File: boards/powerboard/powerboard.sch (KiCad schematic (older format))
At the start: 39 parts, among them J101 RXSM experiment connector, J102 Powerboard <-> Mainboard, J103 Cameraboard, J104 BLDC Motor, J105 BOOST, J106 Boost24V_EN, J107 24V_1, J108 24V_2, J109 24V_3, J110 BAT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

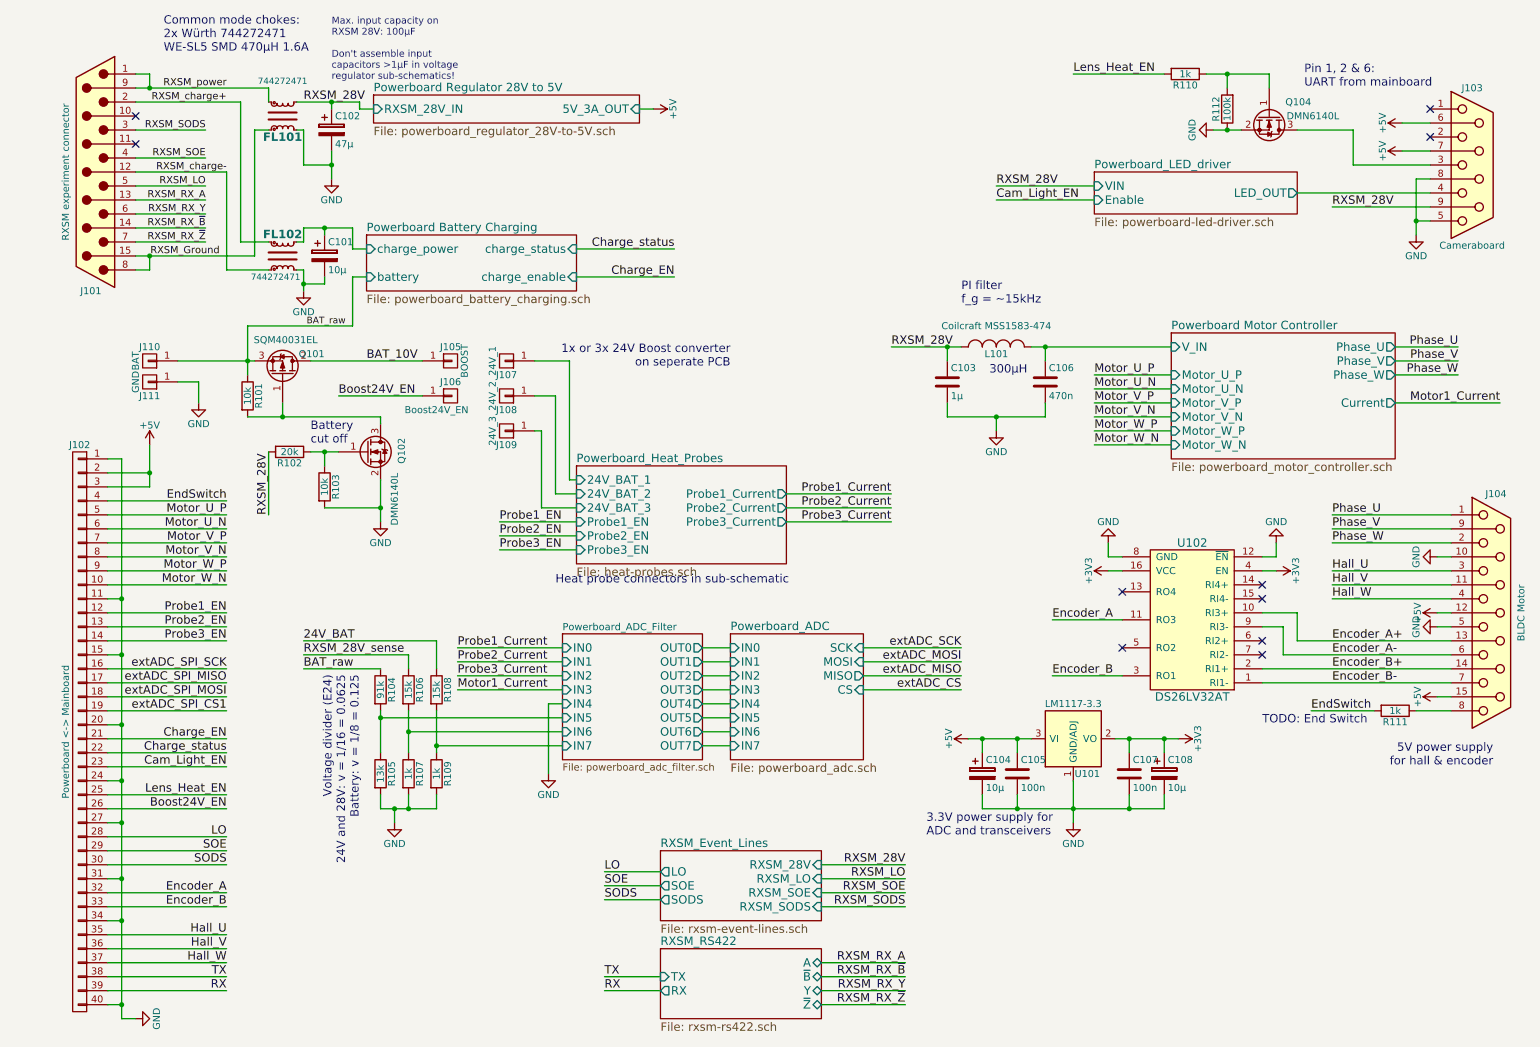
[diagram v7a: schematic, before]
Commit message: [powerboard] layout: parts placed; RS-422 termination added; various minor improvements
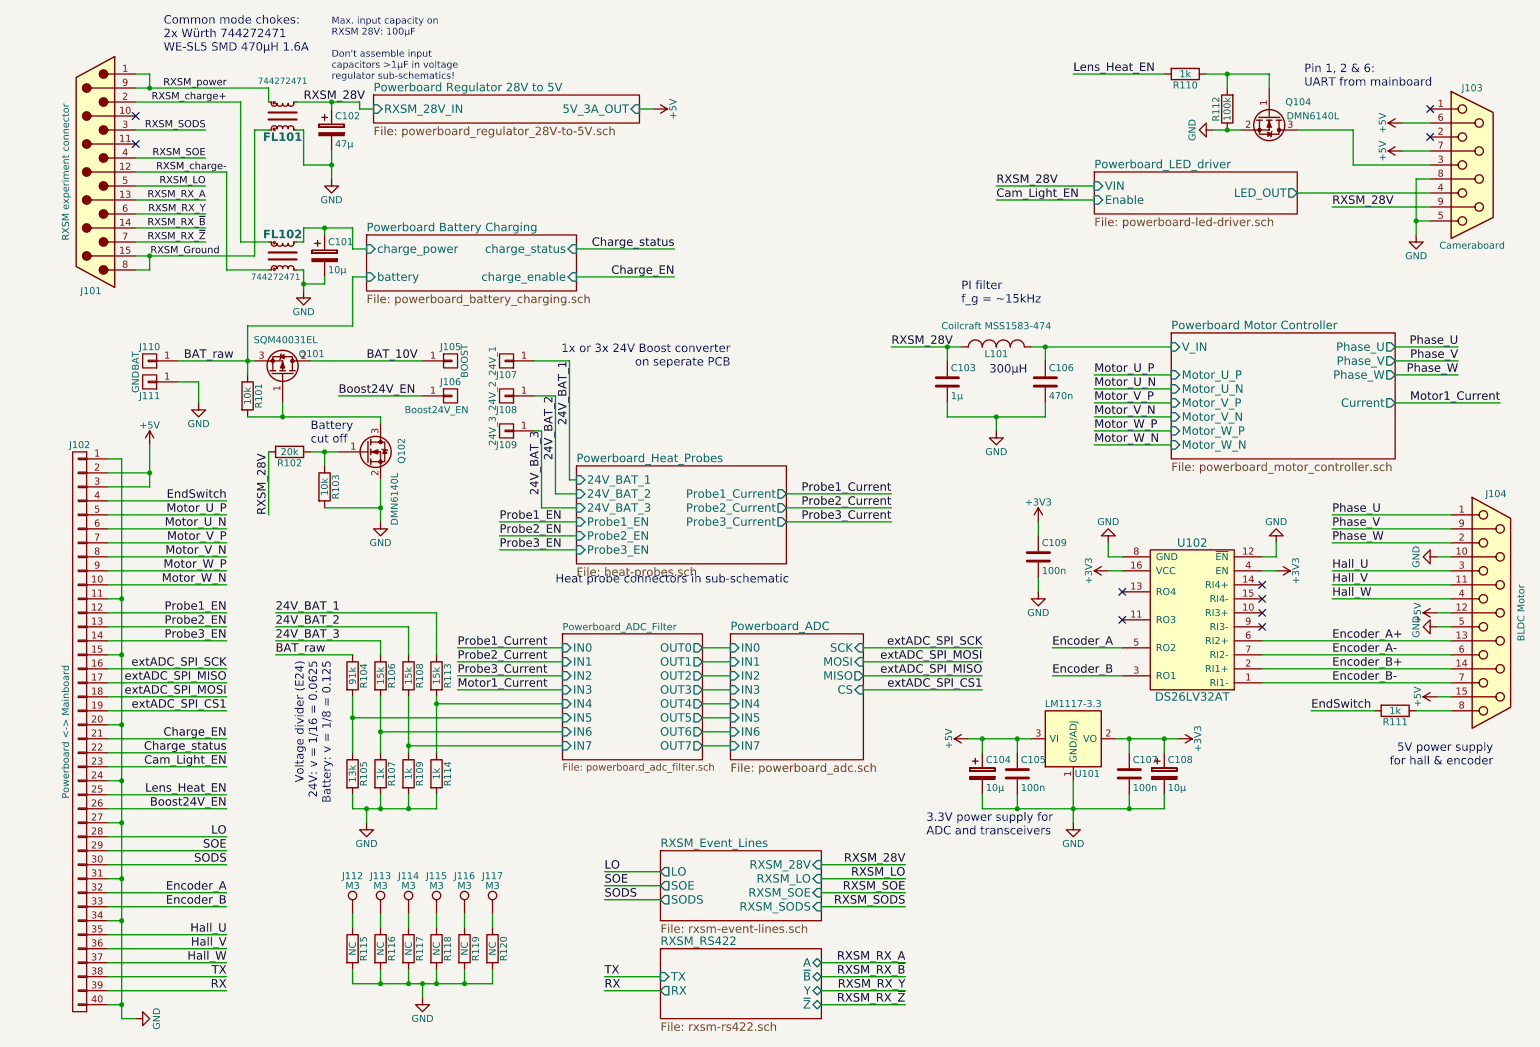
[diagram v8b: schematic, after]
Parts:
- added C109: 100n, Capacitors_SMD:C_0603, symbol C
- added J112, J113, J114, J115, J116, J117: M3, Mounting_Holes:MountingHole_3.2mm_M3_Pad, symbol TEST_1P
- added R113: 15k, Resistors_SMD:R_0603, symbol R
- added R114: 1k, Resistors_SMD:R_0603, symbol R
- added R115, R116, R117, R118, R119, R120: NC, Resistors_SMD:R_0603, symbol R
- J101: footprint Connectors:DB9MD -> Connectors:DB15MD
- U101: footprint TO_SOT_Packages_SMD:SOT-223-3Lead_TabPin2 -> TO_SOT_Packages_SMD:SOT-223
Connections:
- net Powerboard_Heat_Probes/24V_BAT_2 is gone; now on net 24V_BAT_2: J108.1 (P1)
- net RXSM_28V_sense is gone; now on net 24V_BAT_3: R106.1
- net +3V3: now also C109.1
- net Encoder_A: now also U102.5 (RO2); no longer U102.11 (RO3)
- net Encoder_A+: now also U102.6 (RI2+); no longer U102.10 (RI3+)
- net Encoder_A-: now also U102.7 (RI2-); no longer U102.9 (RI3-)
- net GND: now also C109.2, R114.2, R115.2, R116.2, R117.2, R118.2, R119.2, R120.2
- net 24V_BAT renamed 24V_BAT_2
- net Powerboard_Heat_Probes/24V_BAT_1 renamed 24V_BAT_1
- net 24V_BAT_1: now also R113.1
- net Powerboard_Heat_Probes/24V_BAT_3 renamed 24V_BAT_3
- new net: J112.1, R115.1
- new net: J113.1, R116.1
- new net: J114.1, R117.1
- new net: J115.1, R118.1
- new net: J116.1, R119.1
- new net: J117.1, R120.1
- new net Powerboard_ADC_Filter/IN4: R113.2, R114.1
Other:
- note added: "Voltage divider (E24)\n24V: v = 1/16 = 0.0625\nBattery: v = 1/8 = 0.125"
- note removed: "TODO: End Switch"
- note removed: "Voltage divider (E24)\n24V and 28V: v = 1/16 = 0.0625\nBattery: v = 1/8 = 0.125"
- moved on the sheet: R104, R105, R106, R107, R108, R109
